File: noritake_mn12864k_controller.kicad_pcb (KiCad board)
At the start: 4 copper layers, 85 x 45.5 mm, 148 parts, among them J1 Conn_01x11, J2 USB_C_Receptacle_USB2.0, J3 TagConnect_TC2030_SWD, J4 Conn_01x18, Q1 AO3400A, Q10 2N7002, Q11 LBSS84LT1G, Q12 2N7002, Q13 TO-252, Q14 CJT04N15, Q15 2N7002, Q16 LBSS84LT1G, Q17 2N7002, Q18 S9015, Q2 AO3400A, Q3 S9015, Q4 AO3401A, Q5 AO3401A, Q6 S9015, Q7 2N7002, Q8 LBSS84LT1G, Q9 2N7002, T1 Wuerth 760390013, T2 Wuerth 760390013, T3 Wuerth 760390013, U1 SN74AVC8T245PW, U10 SRV05-4, U11 SRV05-4, U12 SRV05-4, U2 74HC14, U3 CD4051B, U4 MN12864K, U5 STM32F730R8T6, U6 NE555D, U7 74HC08, U8 SRV05-4, U9 XC6206PxxxMR

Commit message: Fix FFC courtyard
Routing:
- net GND: vias 54 -> 61
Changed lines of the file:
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@@
     (thickness 1.6)
     (drawings 5)
-    (tracks 1404)
+    (tracks 1411)
     (zones 0)
     (modules 148)
@@
     (add_net VDD2)
   )
+  (module Connector_FFC:MINTRON-LW05202-18 (layer F.Cu)
+    (at 152.6 135.8 180)
+    (attr smd)
+    (fp_text reference J4 (at 0 0.8) (layer F.SilkS)
+      (effects (font (size 1 1) (thickness 0.15)))
+    )
+    (fp_text value Conn_01x18 (at 0 -0.5) (layer F.Fab)
+      (effects (font (size 1 1) (thickness 0.15)))
+    )
+    (fp_line (start -7.4 0.1) (end 7.4 0.1) (layer F.CrtYd) (width 0.05))
+    (fp_line (start 7.4 0.1) (end 7.4 -6.2) (layer F.CrtYd) (width 0.05))
+    (fp_line (start 7.4 -6.2) (end -7.4 -6.2) (layer F.CrtYd) (width 0.05))
+    (fp_line (start -7.4 -6.2) (end -7.4 0.1) (layer F.CrtYd) (width 0.05))
+    (fp_line (start 7.4 -4.65) (end -7.4 -4.65) (layer F.SilkS) (width 0.12))
+    (fp_line (start -7.2 -1) (end -4.6 -1) (layer F.SilkS) (width 0.12))
+    (fp_line (start -4.6 -1) (end -4.6 -0.1) (layer F.SilkS) (width 0.12))
+    (fp_line (start 7.2 -1) (end 4.6 -1) (layer F.SilkS) (width 0.12))
+    (fp_line (start 4.6 -1) (end 4.6 -0.7) (layer F.SilkS) (width 0.12))
+    (pad MP smd rect (at -6.05 -2.8 180) (size 2.5 3.2) (layers F.Cu F.Paste F.Mask)
+      (net 5 GND))
+    (pad MP smd rect (at 6.05 -2.8 180) (size 2.5 3.2) (layers F.Cu F.Paste F.Mask)
+      (net 5 GND))
+    (pad 18 smd rect (at 4.25 -0.9 180) (size 0.3 1.8) (layers F.Cu F.Paste F.Mask)
+      (net 5 GND))
+    (pad 17 smd rect (at 3.75 -0.9 180) (size 0.3 1.8) (layers F.Cu F.Paste F.Mask)
+      (net 107 /DBG15))
+    (pad 16 smd rect (at 3.25 -0.9 180) (size 0.3 1.8) (layers F.Cu F.Paste F.Mask)
+      (net 106 /DBG14))
+    (pad 15 smd rect (at 2.75 -0.9 180) (size 0.3 1.8) (layers F.Cu F.Paste F.Mask)
+      (net 105 /DBG13))
+    (pad 14 smd rect (at 2.25 -0.9 180) (size 0.3 1.8) (layers F.Cu F.Paste F.Mask)
+      (net 104 /DBG12))
+    (pad 13 smd rect (at 1.75 -0.9 180) (size 0.3 1.8) (layers F.Cu F.Paste F.Mask)
+      (net 103 /DBG11))
+    (pad 12 smd rect (at 1.25 -0.9 180) (size 0.3 1.8) (layers F.Cu F.Paste F.Mask)
+      (net 102 /DBG10))
+    (pad 11 smd rect (at 0.75 -0.9 180) (size 0.3 1.8) (layers F.Cu F.Paste F.Mask)
+      (net 101 /DBG09))
+    (pad 10 smd rect (at 0.25 -0.9 180) (size 0.3 1.8) (layers F.Cu F.Paste F.Mask)
+      (net 100 /DBG08))
+    (pad 9 smd rect (at -0.25 -0.9 180) (size 0.3 1.8) (layers F.Cu F.Paste F.Mask)
+      (net 99 /DBG07))
+    (pad 8 smd rect (at -0.75 -0.9 180) (size 0.3 1.8) (layers F.Cu F.Paste F.Mask)
+      (net 98 /DBG06))
+    (pad 7 smd rect (at -1.25 -0.9 180) (size 0.3 1.8) (layers F.Cu F.Paste F.Mask)
+      (net 108 /DBG05))
+    (pad 6 smd rect (at -1.75 -0.9 180) (size 0.3 1.8) (layers F.Cu F.Paste F.Mask)
+      (net 112 /DBG04))
+    (pad 5 smd rect (at -2.25 -0.9 180) (size 0.3 1.8) (layers F.Cu F.Paste F.Mask)
+      (net 111 /DBG03))
+    (pad 4 smd rect (at -2.75 -0.9 180) (size 0.3 1.8) (layers F.Cu F.Paste F.Mask)
+      (net 110 /DBG02))
+    (pad 3 smd rect (at -3.25 -0.9 180) (size 0.3 1.8) (layers F.Cu F.Paste F.Mask)
+      (net 109 /DBG01))
+    (pad 2 smd rect (at -3.75 -0.9 180) (size 0.3 1.8) (layers F.Cu F.Paste F.Mask)
+      (net 97 /DBG00))
+    (pad 1 smd rect (at -4.25 -0.9 180) (size 0.3 1.8) (layers F.Cu F.Paste F.Mask)
+      (net 5 GND))
+  )
   (module Resistor_SMD:R_0805_2012Metric (layer F.Cu)
     (at 142.9 100.7 180)
@@
     )
   )
-  (module Connector_FFC:MINTRON-LW05202-18 (layer F.Cu)
-    (at 152.6 135.8 180)
-    (attr smd)
-    (fp_text reference J4 (at 0 0.8) (layer F.SilkS)
-      (effects (font (size 1 1) (thickness 0.15)))
-    )
-    (fp_text value Conn_01x18 (at 0 -0.5) (layer F.Fab)
-      (effects (font (size 1 1) (thickness 0.15)))
-    )
-    (fp_line (start 4.6 -1) (end 4.6 -0.7) (layer F.SilkS) (width 0.12))
-    (fp_line (start 7.2 -1) (end 4.6 -1) (layer F.SilkS) (width 0.12))
-    (fp_line (start -4.6 -1) (end -4.6 -0.1) (layer F.SilkS) (width 0.12))
-    (fp_line (start -7.2 -1) (end -4.6 -1) (layer F.SilkS) (width 0.12))
-    (fp_line (start 7.4 -4.65) (end -7.4 -4.65) (layer F.SilkS) (width 0.12))
-    (fp_line (start -7.4 -6.2) (end -7.4 0.1) (layer Dwgs.User) (width 0.05))
-    (fp_line (start 7.4 -6.2) (end -7.4 -6.2) (layer Dwgs.User) (width 0.05))
-    (fp_line (start 7.4 0.1) (end 7.4 -6.2) (layer Dwgs.User) (width 0.05))
-    (fp_line (start -7.4 0.1) (end 7.4 0.1) (layer F.CrtYd) (width 0.05))
-    (pad 1 smd rect (at -4.25 -0.9 180) (size 0.3 1.8) (layers F.Cu F.Paste F.Mask)
-      (net 5 GND))
-    (pad 2 smd rect (at -3.75 -0.9 180) (size 0.3 1.8) (layers F.Cu F.Paste F.Mask)
-      (net 97 /DBG00))
-    (pad 3 smd rect (at -3.25 -0.9 180) (size 0.3 1.8) (layers F.Cu F.Paste F.Mask)
-      (net 109 /DBG01))
-    (pad 4 smd rect (at -2.75 -0.9 180) (size 0.3 1.8) (layers F.Cu F.Paste F.Mask)
-      (net 110 /DBG02))
-    (pad 5 smd rect (at -2.25 -0.9 180) (size 0.3 1.8) (layers F.Cu F.Paste F.Mask)
-      (net 111 /DBG03))
-    (pad 6 smd rect (at -1.75 -0.9 180) (size 0.3 1.8) (layers F.Cu F.Paste F.Mask)
-      (net 112 /DBG04))
-    (pad 7 smd rect (at -1.25 -0.9 180) (size 0.3 1.8) (layers F.Cu F.Paste F.Mask)
-      (net 108 /DBG05))
-    (pad 8 smd rect (at -0.75 -0.9 180) (size 0.3 1.8) (layers F.Cu F.Paste F.Mask)
-      (net 98 /DBG06))
-    (pad 9 smd rect (at -0.25 -0.9 180) (size 0.3 1.8) (layers F.Cu F.Paste F.Mask)
-      (net 99 /DBG07))
-    (pad 10 smd rect (at 0.25 -0.9 180) (size 0.3 1.8) (layers F.Cu F.Paste F.Mask)
-      (net 100 /DBG08))
-    (pad 11 smd rect (at 0.75 -0.9 180) (size 0.3 1.8) (layers F.Cu F.Paste F.Mask)
-      (net 101 /DBG09))
-    (pad 12 smd rect (at 1.25 -0.9 180) (size 0.3 1.8) (layers F.Cu F.Paste F.Mask)
-      (net 102 /DBG10))
-    (pad 13 smd rect (at 1.75 -0.9 180) (size 0.3 1.8) (layers F.Cu F.Paste F.Mask)
-      (net 103 /DBG11))
-    (pad 14 smd rect (at 2.25 -0.9 180) (size 0.3 1.8) (layers F.Cu F.Paste F.Mask)
-      (net 104 /DBG12))
-    (pad 15 smd rect (at 2.75 -0.9 180) (size 0.3 1.8) (layers F.Cu F.Paste F.Mask)
-      (net 105 /DBG13))
-    (pad 16 smd rect (at 3.25 -0.9 180) (size 0.3 1.8) (layers F.Cu F.Paste F.Mask)
-      (net 106 /DBG14))
-    (pad 17 smd rect (at 3.75 -0.9 180) (size 0.3 1.8) (layers F.Cu F.Paste F.Mask)
-      (net 107 /DBG15))
-    (pad 18 smd rect (at 4.25 -0.9 180) (size 0.3 1.8) (layers F.Cu F.Paste F.Mask)
-      (net 5 GND))
-    (pad MP smd rect (at 6.05 -2.8 180) (size 2.5 3.2) (layers F.Cu F.Paste F.Mask)
-      (net 5 GND))
-    (pad MP smd rect (at -6.05 -2.8 180) (size 2.5 3.2) (layers F.Cu F.Paste F.Mask)
-      (net 5 GND))
-  )
   (module VFD_Noritake:MN12864K (layer B.Cu)
     (at 178 98.5 180)
@@
   (segment (start 133.660589 130.139411) (end 134.2 129.6) (width 0.127) (layer F.Cu) (net 5))
   (segment (start 133.639411 130.139411) (end 133.660589 130.139411) (width 0.127) (layer F.Cu) (net 5))
-  (via (at 117.6 126.975) (size 0.45) (drill 0.2) (layers F.Cu B.Cu) (net 5))
+  (via (at 117.5 127.1) (size 0.45) (drill 0.2) (layers F.Cu B.Cu) (net 5))
   (segment (start 117.610589 126.964411) (end 117.6 126.975) (width 0.127) (layer F.Cu) (net 5))
   (segment (start 117.610589 126.189411) (end 117.610589 126.964411) (width 0.127) (layer F.Cu) (net 5))
@@
   (segment (start 159.96 114.5) (end 158.3 114.5) (width 0.25) (layer F.Cu) (net 5))
   (segment (start 158.3 114.5) (end 157.8 114) (width 0.25) (layer F.Cu) (net 5))
+  (via (at 119 132.6) (size 0.45) (drill 0.2) (layers F.Cu B.Cu) (net 5))
+  (via (at 119.9 134.8) (size 0.45) (drill 0.2) (layers F.Cu B.Cu) (net 5))
+  (via (at 125.1 132.5) (size 0.45) (drill 0.2) (layers F.Cu B.Cu) (net 5))
+  (via (at 125.1 130.7) (size 0.45) (drill 0.2) (layers F.Cu B.Cu) (net 5))
+  (via (at 123.8 129) (size 0.45) (drill 0.2) (layers F.Cu B.Cu) (net 5))
+  (via (at 121.6 130.7) (size 0.45) (drill 0.2) (layers F.Cu B.Cu) (net 5))
+  (via (at 123.5 127.1) (size 0.45) (drill 0.2) (layers F.Cu B.Cu) (net 5))
   (segment (start 145.32 123.3) (end 144.75 123.3) (width 0.5) (layer F.Cu) (net 6))
   (segment (start 144.4 123.3) (end 144.2 123.5) (width 0.5) (layer F.Cu) (net 6))

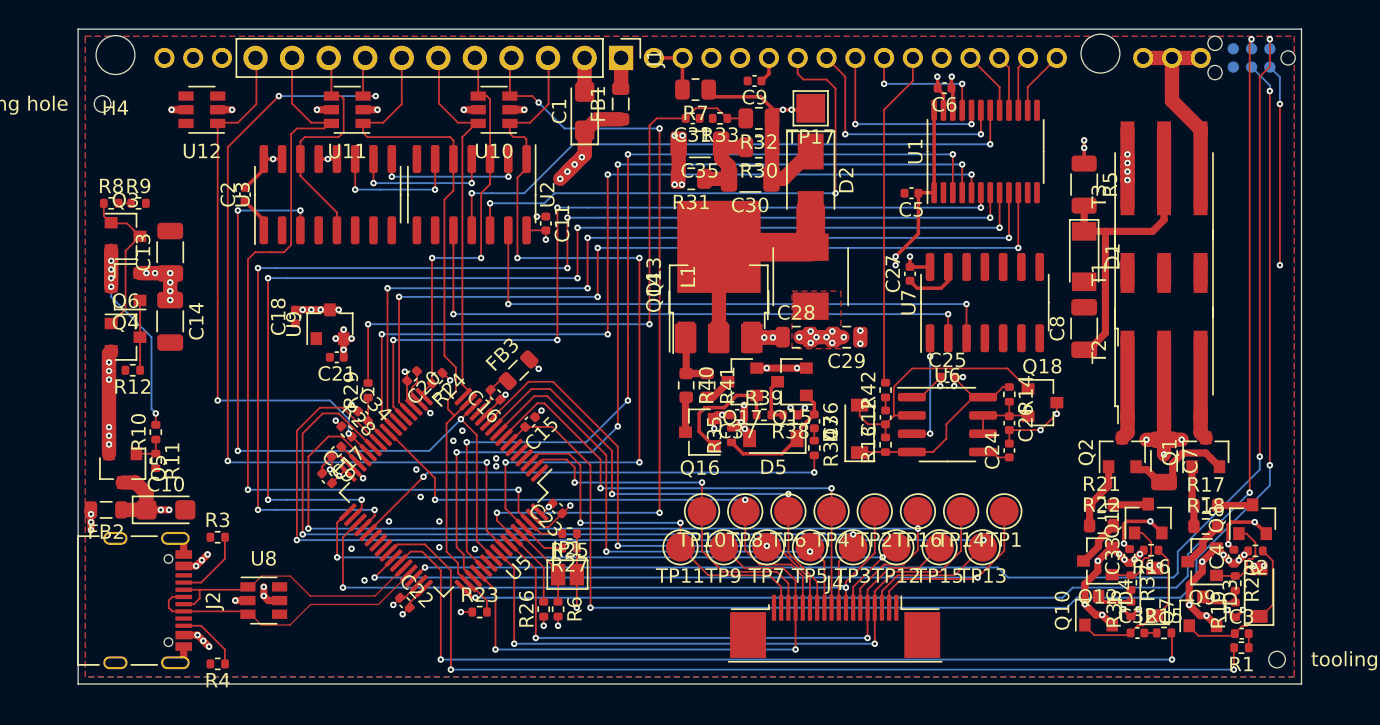
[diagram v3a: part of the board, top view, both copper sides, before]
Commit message: Add some via stitching
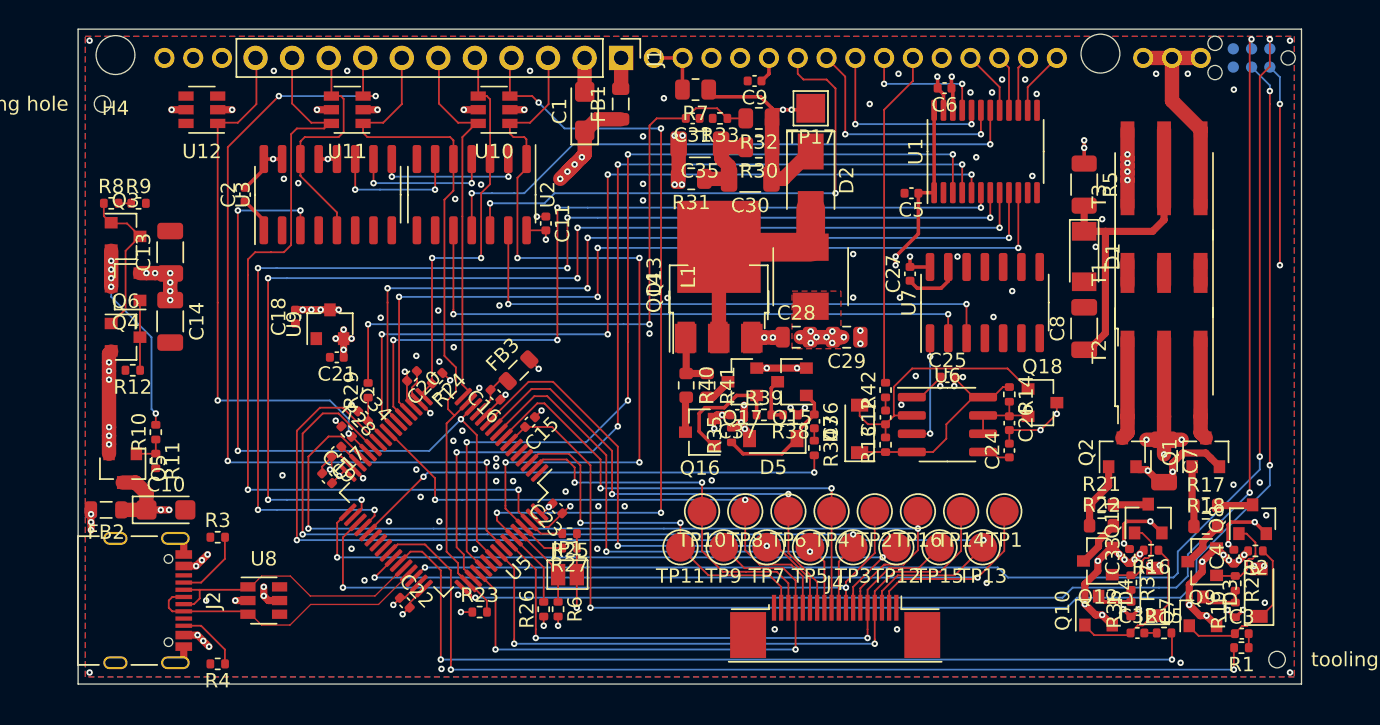
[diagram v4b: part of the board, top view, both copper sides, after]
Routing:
- net GND: vias 61 -> 128
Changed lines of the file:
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@@
     (thickness 1.6)
     (drawings 5)
-    (tracks 1411)
+    (tracks 1483)
     (zones 0)
     (modules 148)
@@
   (segment (start 178.35 125.95) (end 176.75 125.95) (width 0.5) (layer F.Cu) (net 5))
   (segment (start 176.75 125.95) (end 176.05 126.65) (width 0.5) (layer F.Cu) (net 5))
-  (segment (start 176.05 126.65) (end 176.05 128.2) (width 0.5) (layer F.Cu) (net 5))
+  (segment (start 176.05 126.65) (end 176.05 127.25) (width 0.5) (layer F.Cu) (net 5))
   (segment (start 175.45 127.975) (end 175.125 127.975) (width 0.5) (layer F.Cu) (net 5))
-  (segment (start 175.125 127.975) (end 174.25 127.1) (width 0.5) (layer F.Cu) (net 5))
+  (segment (start 175.125 127.975) (end 174.325 127.175) (width 0.5) (layer F.Cu) (net 5))
   (segment (start 174.25 127.1) (end 173.65 127.1) (width 0.5) (layer F.Cu) (net 5))
   (via (at 181.7 133.8) (size 0.45) (drill 0.2) (layers F.Cu B.Cu) (net 5))
@@
   (via (at 133.35 137.95) (size 0.45) (drill 0.2) (layers F.Cu B.Cu) (net 5))
   (segment (start 133.35 137.31) (end 133.35 137.95) (width 0.127) (layer F.Cu) (net 5))
-  (via (at 134.2 129.6) (size 0.45) (drill 0.2) (layers F.Cu B.Cu) (net 5))
+  (via (at 134.2 129.65) (size 0.45) (drill 0.2) (layers F.Cu B.Cu) (net 5))
   (segment (start 133.660589 130.139411) (end 134.2 129.6) (width 0.127) (layer F.Cu) (net 5))
   (segment (start 133.639411 130.139411) (end 133.660589 130.139411) (width 0.127) (layer F.Cu) (net 5))
@@
   (via (at 121.6 130.7) (size 0.45) (drill 0.2) (layers F.Cu B.Cu) (net 5))
   (via (at 123.5 127.1) (size 0.45) (drill 0.2) (layers F.Cu B.Cu) (net 5))
+  (via (at 182.1 128) (size 0.45) (drill 0.2) (layers F.Cu B.Cu) (net 5))
+  (via (at 128 107.3) (size 0.45) (drill 0.2) (layers F.Cu B.Cu) (net 5))
+  (via (at 126.2 108.3) (size 0.45) (drill 0.2) (layers F.Cu B.Cu) (net 5))
+  (via (at 126.1 118.6) (size 0.45) (drill 0.2) (layers F.Cu B.Cu) (net 5))
+  (via (at 114.3 106.9) (size 0.45) (drill 0.2) (layers F.Cu B.Cu) (net 5))
+  (via (at 115.3 107.2) (size 0.45) (drill 0.2) (layers F.Cu B.Cu) (net 5))
+  (via (at 100.8 97.3) (size 0.45) (drill 0.2) (layers F.Cu B.Cu) (net 5))
+  (via (at 184.2 97.3) (size 0.45) (drill 0.2) (layers F.Cu B.Cu) (net 5))
+  (via (at 184.2 141.2) (size 0.45) (drill 0.2) (layers F.Cu B.Cu) (net 5))
+  (via (at 100.8 141.2) (size 0.45) (drill 0.2) (layers F.Cu B.Cu) (net 5))
+  (via (at 108.9 136.2) (size 0.45) (drill 0.2) (layers F.Cu B.Cu) (net 5))
+  (via (at 114.2 127.5) (size 0.45) (drill 0.2) (layers F.Cu B.Cu) (net 5))
+  (via (at 113.6 99.4) (size 0.45) (drill 0.2) (layers F.Cu B.Cu) (net 5))
+  (via (at 118.7 99.4) (size 0.45) (drill 0.2) (layers F.Cu B.Cu) (net 5))
+  (via (at 131.4 99.4) (size 0.45) (drill 0.2) (layers F.Cu B.Cu) (net 5))
+  (via (at 165.8 100) (size 0.45) (drill 0.2) (layers F.Cu B.Cu) (net 5))
+  (via (at 164.2 100) (size 0.45) (drill 0.2) (layers F.Cu B.Cu) (net 5))
+  (via (at 180.3 100.7) (size 0.45) (drill 0.2) (layers F.Cu B.Cu) (net 5))
+  (via (at 177.1 99.6) (size 0.45) (drill 0.2) (layers F.Cu B.Cu) (net 5))
+  (via (at 174.9 99.6) (size 0.45) (drill 0.2) (layers F.Cu B.Cu) (net 5))
+  (segment (start 176.05 127.25) (end 176.05 128.2) (width 0.5) (layer F.Cu) (net 5))
+  (via (at 176.05 127.25) (size 0.45) (drill 0.2) (layers F.Cu B.Cu) (net 5))
+  (segment (start 174.325 127.175) (end 174.25 127.1) (width 0.5) (layer F.Cu) (net 5))
+  (via (at 174.325 127.175) (size 0.45) (drill 0.2) (layers F.Cu B.Cu) (net 5))
+  (via (at 157.2 122.6) (size 0.45) (drill 0.2) (layers F.Cu B.Cu) (net 5))
+  (via (at 158.2 120.6) (size 0.45) (drill 0.2) (layers F.Cu B.Cu) (net 5))
+  (via (at 148.4 138.2) (size 0.45) (drill 0.2) (layers F.Cu B.Cu) (net 5))
+  (via (at 156.9 138.2) (size 0.45) (drill 0.2) (layers F.Cu B.Cu) (net 5))
+  (via (at 126.4 135.8) (size 0.45) (drill 0.2) (layers F.Cu B.Cu) (net 5))
+  (via (at 123.5 119.2) (size 0.45) (drill 0.2) (layers F.Cu B.Cu) (net 5))
+  (via (at 125.025 116.05) (size 0.45) (drill 0.2) (layers F.Cu B.Cu) (net 5))
+  (via (at 125.1 119.6) (size 0.45) (drill 0.2) (layers F.Cu B.Cu) (net 5))
+  (via (at 129.05 127.9) (size 0.45) (drill 0.2) (layers F.Cu B.Cu) (net 5))
+  (via (at 133.875 128.625) (size 0.45) (drill 0.2) (layers F.Cu B.Cu) (net 5))
+  (via (at 130.225 127.9) (size 0.45) (drill 0.2) (layers F.Cu B.Cu) (net 5))
+  (via (at 144.025 127.85) (size 0.45) (drill 0.2) (layers F.Cu B.Cu) (net 5))
+  (via (at 136.15 129.65) (size 0.45) (drill 0.2) (layers F.Cu B.Cu) (net 5))
+  (via (at 137.975 129.65) (size 0.45) (drill 0.2) (layers F.Cu B.Cu) (net 5))
+  (via (at 136.075 132.6) (size 0.45) (drill 0.2) (layers F.Cu B.Cu) (net 5))
+  (via (at 163.125 134.975) (size 0.45) (drill 0.2) (layers F.Cu B.Cu) (net 5))
+  (via (at 127.875 121.425) (size 0.45) (drill 0.2) (layers F.Cu B.Cu) (net 5))
+  (via (at 170.7 111.625) (size 0.45) (drill 0.2) (layers F.Cu B.Cu) (net 5))
+  (via (at 171.15 109.7) (size 0.45) (drill 0.2) (layers F.Cu B.Cu) (net 5))
+  (via (at 180.275 128.15) (size 0.45) (drill 0.2) (layers F.Cu B.Cu) (net 5))
+  (via (at 182.55 130.275) (size 0.45) (drill 0.2) (layers F.Cu B.Cu) (net 5))
+  (via (at 182.45 136.35) (size 0.45) (drill 0.2) (layers F.Cu B.Cu) (net 5))
+  (via (at 176.6 140.525) (size 0.45) (drill 0.2) (layers F.Cu B.Cu) (net 5))
+  (via (at 125.25 140.95) (size 0.45) (drill 0.2) (layers F.Cu B.Cu) (net 5))
+  (via (at 121.025 116.55) (size 0.45) (drill 0.2) (layers F.Cu B.Cu) (net 5))
+  (via (at 139.7 117.65) (size 0.45) (drill 0.2) (layers F.Cu B.Cu) (net 5))
+  (via (at 140.7 101.3) (size 0.45) (drill 0.2) (layers F.Cu B.Cu) (net 5))
+  (via (at 139.25 103.95) (size 0.45) (drill 0.2) (layers F.Cu B.Cu) (net 5))
+  (via (at 139.25 107.25) (size 0.45) (drill 0.2) (layers F.Cu B.Cu) (net 5))
+  (via (at 139.25 108.4) (size 0.45) (drill 0.2) (layers F.Cu B.Cu) (net 5))
+  (via (at 129.275 115.7) (size 0.45) (drill 0.2) (layers F.Cu B.Cu) (net 5))
+  (via (at 140.95 115.175) (size 0.45) (drill 0.2) (layers F.Cu B.Cu) (net 5))
+  (via (at 153.85 112.125) (size 0.45) (drill 0.2) (layers F.Cu B.Cu) (net 5))
+  (via (at 153.85 115.15) (size 0.45) (drill 0.2) (layers F.Cu B.Cu) (net 5))
+  (via (at 157.1 115.15) (size 0.45) (drill 0.2) (layers F.Cu B.Cu) (net 5))
+  (via (at 162.4 105.4) (size 0.45) (drill 0.2) (layers F.Cu B.Cu) (net 5))
+  (via (at 166.3 106.7) (size 0.45) (drill 0.2) (layers F.Cu B.Cu) (net 5))
+  (via (at 166.6 101) (size 0.45) (drill 0.2) (layers F.Cu B.Cu) (net 5))
+  (via (at 161.1 112.3) (size 0.45) (drill 0.2) (layers F.Cu B.Cu) (net 5))
+  (via (at 164.9 114.7) (size 0.45) (drill 0.2) (layers F.Cu B.Cu) (net 5))
+  (via (at 163.6 116.5) (size 0.45) (drill 0.2) (layers F.Cu B.Cu) (net 5))
+  (via (at 157 99.6) (size 0.45) (drill 0.2) (layers F.Cu B.Cu) (net 5))
+  (via (at 155 101.7) (size 0.45) (drill 0.2) (layers F.Cu B.Cu) (net 5))
+  (via (at 162 100.9) (size 0.45) (drill 0.2) (layers F.Cu B.Cu) (net 5))
+  (via (at 163.5 100.9) (size 0.45) (drill 0.2) (layers F.Cu B.Cu) (net 5))
   (segment (start 145.32 123.3) (end 144.75 123.3) (width 0.5) (layer F.Cu) (net 6))
   (segment (start 144.4 123.3) (end 144.2 123.5) (width 0.5) (layer F.Cu) (net 6))
@@
   (segment (start 131.55 101.15) (end 132 101.6) (width 0.127) (layer F.Cu) (net 18))
   (segment (start 130 101.15) (end 131.55 101.15) (width 0.127) (layer F.Cu) (net 18))
-  (segment (start 133.8 103.4) (end 140.4 103.4) (width 0.127) (layer B.Cu) (net 18))
-  (via (at 140.4 103.4) (size 0.45) (drill 0.2) (layers F.Cu B.Cu) (net 18))
+  (via (at 140.5 103.4) (size 0.45) (drill 0.2) (layers F.Cu B.Cu) (net 18))
   (segment (start 132 101.6) (end 133.8 103.4) (width 0.127) (layer B.Cu) (net 18))
-  (via (at 140.4 130.1) (size 0.45) (drill 0.2) (layers F.Cu B.Cu) (net 18))
-  (segment (start 140.4 103.4) (end 140.4 130.1) (width 0.127) (layer F.Cu) (net 18))
+  (via (at 140.5 130.1) (size 0.45) (drill 0.2) (layers F.Cu B.Cu) (net 18))
+  (segment (start 140.5 103.4) (end 140.5 130.1) (width 0.127) (layer F.Cu) (net 18))
   (via (at 129.1 130.1) (size 0.45) (drill 0.2) (layers F.Cu B.Cu) (net 18))
   (segment (start 140.4 130.1) (end 129.1 130.1) (width 0.127) (layer B.Cu) (net 18))
@@
   (segment (start 156.8 112.9) (end 183.5 112.9) (width 0.25) (layer Power) (net 7))
   (segment (start 183.5 112.9) (end 183.5 101.7) (width 0.127) (layer F.Cu) (net 7))
+  (segment (start 140.5 103.4) (end 140.3 103.4) (width 0.127) (layer B.Cu) (net 18))
+  (segment (start 140.3 103.4) (end 140.4 103.4) (width 0.127) (layer B.Cu) (net 18))
+  (segment (start 133.8 103.4) (end 140.3 103.4) (width 0.127) (layer B.Cu) (net 18))
+  (segment (start 140.5 130.1) (end 140.4 130.1) (width 0.127) (layer B.Cu) (net 18))
   (via (at 165.325 111.7) (size 0.45) (drill 0.2) (layers F.Cu B.Cu) (net 59))
   (segment (start 165.325 107.8625) (end 165.325 111.7) (width 0.127) (layer F.Cu) (net 59))
